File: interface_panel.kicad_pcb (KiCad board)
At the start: 2 copper layers, 165.1 x 33.4 mm, 48 parts, among them J1 Conn_01x04_Pin, J7 Conn_02x05_Odd_Even, J8 `, Q1 BC547, Q2 BC547, U1 SM420561N, U2 ATmega328P-P, U4 SM420561N, U7 TTP223-BA6, U8 TTP223-BA6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

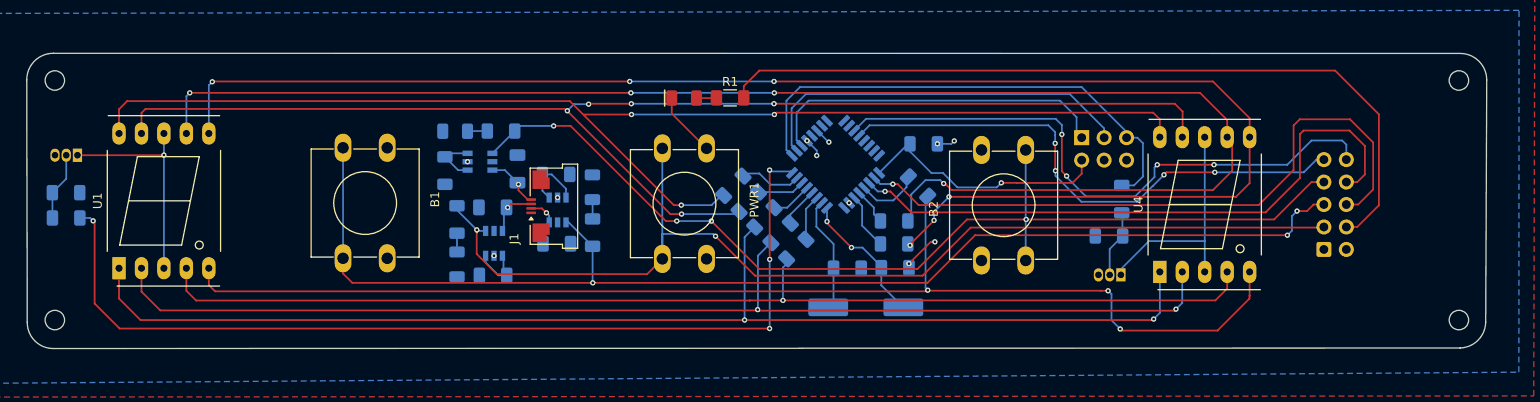
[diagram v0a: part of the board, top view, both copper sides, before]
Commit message: redimensioned
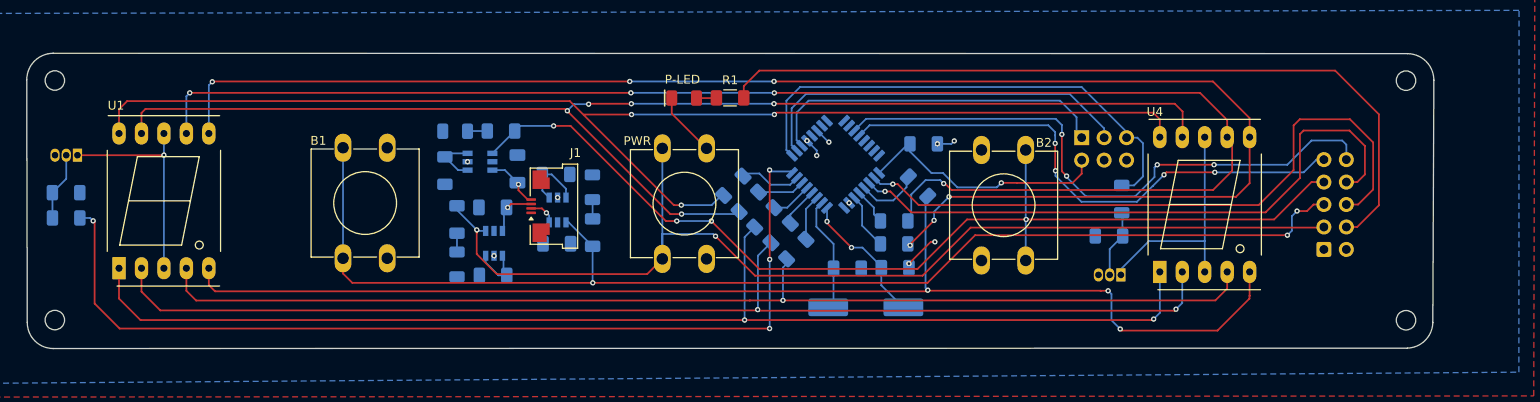
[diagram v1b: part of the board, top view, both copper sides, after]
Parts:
- B1: value SW_Push -> Heater1
- moved H2 5.98 mm to (209.1, 105.4)
- moved H3 5.98 mm to (209.1, 78.3)
- renumbered PWR1 to PWR
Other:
- board size 165.1 x 33.4 mm -> 159.2 x 33.4 mm
- board text added: "P-LED"

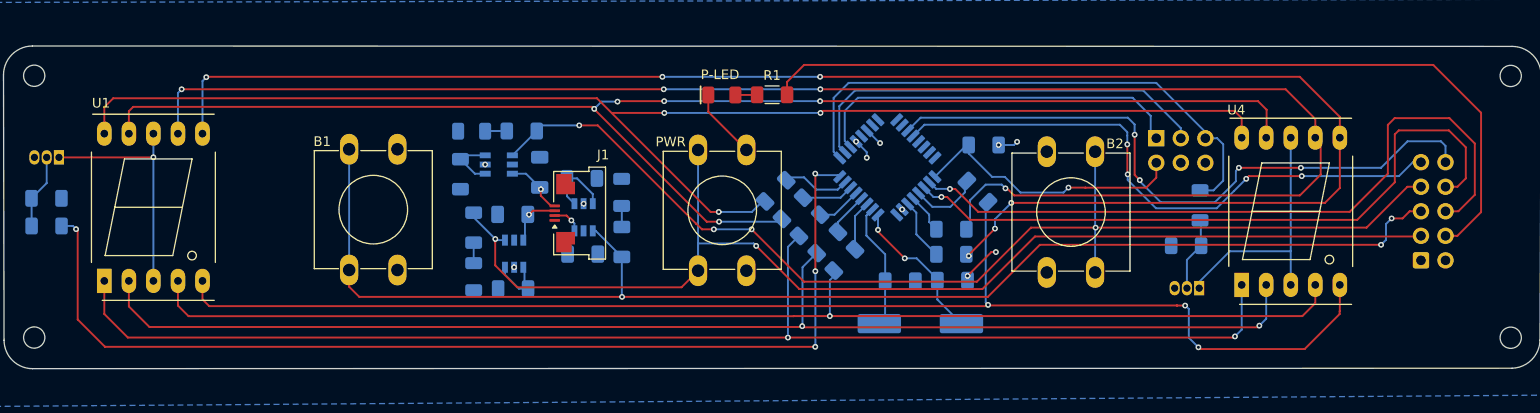
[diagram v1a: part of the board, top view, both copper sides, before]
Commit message: Fixed- schematics -atmega symbol
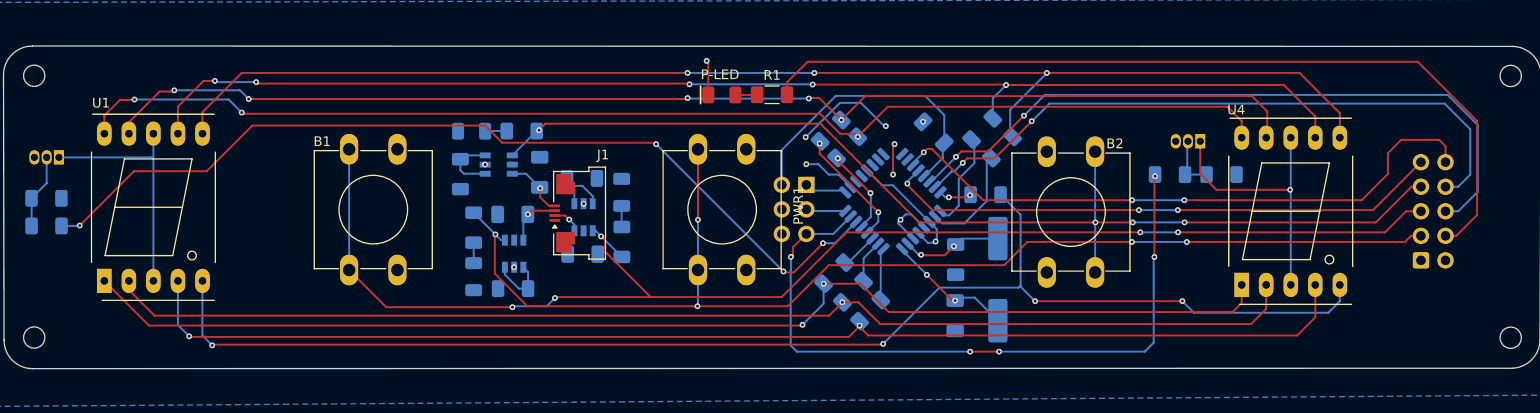
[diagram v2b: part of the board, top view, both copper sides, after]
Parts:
- removed PWR: SW_Push, Button_Switch_THT:SW_PUSH-12mm
- removed U2: ATmega328P-P, atmega328p-smd:QFP80P900X900X120-32N
- added PWR1: SW_Push, Button_Switch_THT:SW_PUSH-12mm, F.Cu at (130.0, 85.9)
- added U3: ATmega328P-A, Package_QFP:TQFP-32_7x7mm_P0.8mm, B.Cu at (145.2, 91.3)
- B1: value Heater1 -> SW_Push
- moved J8 36.5 mm to (136.2, 89.5), turned to 180 degrees
- moved Q2 15.2 mm to (177.0, 85.0)
- moved R8 12.2 mm to (156.4, 85.7), turned to 45 degrees
- moved R7 10.9 mm to (154.4, 83.8), turned to 45 degrees
- moved Y1 9.23 mm to (156.0, 99.3), turned to 90 degrees
- moved R12 8.96 mm to (138.7, 83.9), turned to 45 degrees
- moved R5 8.67 mm to (140.4, 85.7), turned to 45 degrees
- moved R14 8.22 mm to (179.2, 88.5), turned to 180 degrees
- moved C2 6.72 mm to (151.6, 103.1), turned to -90 degrees
- moved R9 5.88 mm to (142.8, 102.5)
- moved R10 5.76 mm to (141.0, 100.6)
- moved R11 5.57 mm to (139.1, 98.7)
- moved R2 5.34 mm to (149.4, 84.1), turned to -45 degrees
- moved R4 4.44 mm to (173.8, 88.5), turned to 0 degrees
- moved C1 2.18 mm to (151.7, 97.3), turned to -90 degrees
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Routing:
- net A: track 170.9 -> 129.4 mm, vias 4 -> 5
- net B: track 174.4 -> 134.0 mm, vias 6 -> 3
- net /miso: track 43.7 -> 4.09 mm
- net D13: track 40.2 -> 4.38 mm
- net F: track 148.1 -> 126.2 mm
- net G: track 144.4 -> 125.5 mm
- net 5V: track 4.18 -> 22.3 mm
- net /mosi: track 57.0 -> 73.1 mm, vias 0 -> 5
- net Net-(U3-PB2): track 109.2 -> 95.0 mm
- net E: track 138.1 -> 126.1 mm
- net D: track 133.4 -> 124.4 mm, vias 2 -> 1
- net Net-(U3-PB0): track 5.35 -> 12.5 mm, vias 0 -> 2
- net GND: track 13.2 -> 20.1 mm, vias 3 -> 4
- net Net-(U3-PD3): track 4.18 -> 10.3 mm
- net Net-(U3-XTAL1/PB6): track 15.9 -> 10.7 mm
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
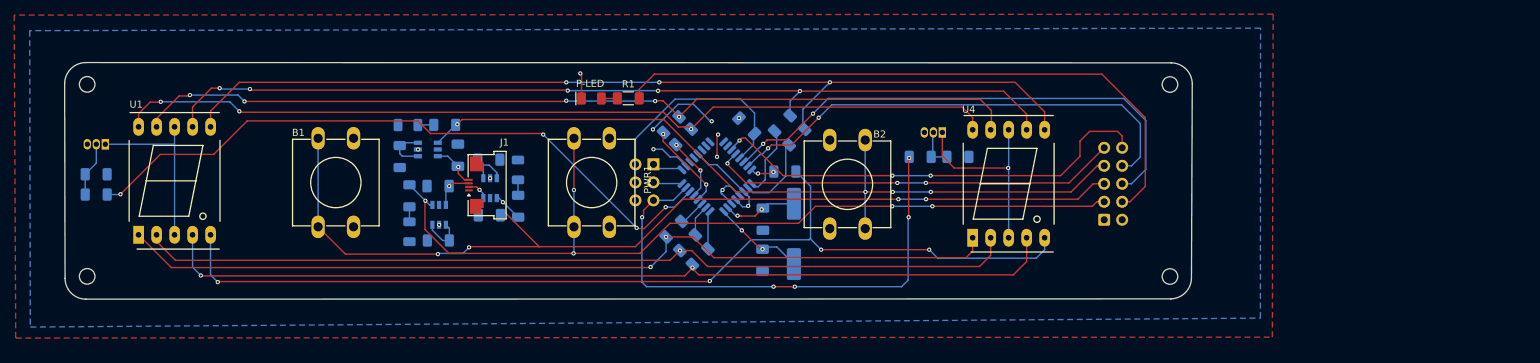
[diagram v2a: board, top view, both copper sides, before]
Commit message: fully routed with TH-atmega
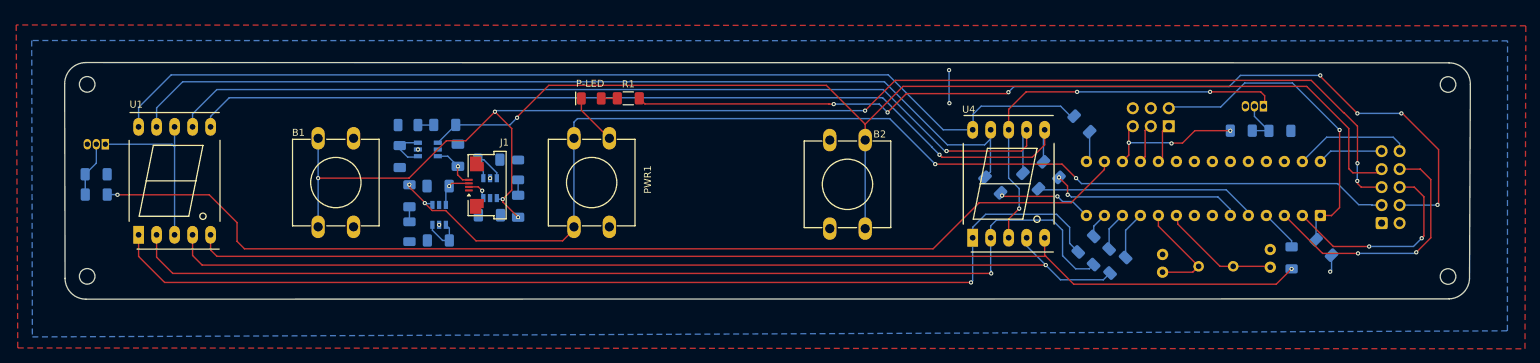
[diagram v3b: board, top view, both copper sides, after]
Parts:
- removed U3: ATmega328P-A, Package_QFP:TQFP-32_7x7mm_P0.8mm
- added U2: ATmega328P-P, Package_DIP:DIP-28_W7.62mm, B.Cu at (230.3, 96.8)
- C1, C2: footprint Capacitor_SMD:C_1206_3216Metric_Pad1.33x1.80mm_HandSolder -> Capacitor_THT:C_Disc_D3.0mm_W2.0mm_P2.50mm
- Y1: footprint Crystal:Crystal_SMD_HC49-SD -> Crystal:Crystal_HC49-U_Vertical
- moved R2 83.2 mm to (230.8, 101.2), turned to 135 degrees
- moved J8 72.9 mm to (208.9, 84.2), turned to 90 degrees
- moved R6 72.6 mm to (226.3, 102.7), turned to -90 degrees
- moved C1 71.9 mm to (223.3, 104.0), turned to 90 degrees
- moved R9 59.0 mm to (201.8, 103.8)
- moved R10 58.4 mm to (199.4, 102.6)
- moved R11 58.2 mm to (197.2, 100.8)
- moved Y1 57.3 mm to (213.2, 103.9), turned to 0 degrees
- moved C2 56.5 mm to (208.1, 104.8), turned to 90 degrees
- moved R5 56.3 mm to (196.7, 83.8), turned to 135 degrees
- moved R12 46.2 mm to (184.1, 92.5), turned to 135 degrees
- moved R14 45.6 mm to (224.6, 84.8)
- moved Q2 45.5 mm to (222.3, 81.3)
- moved R4 45.5 mm to (219.2, 84.8)
- moved H2 39.2 mm to (248.4, 105.4)
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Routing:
- net Net-(U2-PB2): track 95.0 -> 151.2 mm, vias 4 -> 1
- net /K1: track 142.1 -> 197.7 mm, vias 5 -> 7
- net /mosi: track 73.1 -> 21.4 mm, vias 5 -> 3
- net /K2: track 113.7 -> 164.5 mm, vias 4 -> 1
- net /A5: track 58.3 -> 9.26 mm, vias 3 -> 0
- net /A4: track 63.9 -> 17.2 mm, vias 3 -> 0
- net RX: track 72.8 -> 29.1 mm
- net S. LED: track 90.0 -> 133.5 mm, vias 0 -> 7
- net /K3: track 125.1 -> 163.0 mm, vias 5 -> 4
- net TX: track 67.9 -> 37.2 mm
- net Net-(Q2-C): track 28.6 -> 58.5 mm, vias 1 -> 3
- net D: track 124.4 -> 148.7 mm
- net E: track 126.1 -> 149.1 mm, vias 2 -> 1
- net Net-(U2-PD3): track 10.3 -> 31.5 mm
- net DPX: track 140.1 -> 160.3 mm, vias 4 -> 1
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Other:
- board size 159.2 x 33.4 mm -> 198.4 x 33.4 mm

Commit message: dimension plot
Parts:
- moved R6 9.93 mm to (216.7, 105.4)
- moved U2 9.93 mm to (220.8, 99.4)
- moved U4 9.93 mm to (171.7, 102.5)
- moved Y1 9.93 mm to (203.6, 106.6)
- moved J7 9.93 mm to (229.4, 100.5)
- moved PWR1 9.93 mm to (120.4, 88.5)
- moved Q2 9.93 mm to (212.7, 84.0)
- moved R10 9.93 mm to (189.8, 105.2)
- moved R4 9.93 mm to (209.6, 87.4)
- moved R5 9.93 mm to (187.1, 86.5)
- moved C6 9.93 mm to (103.5, 99.4)
- moved D1 9.93 mm to (117.8, 82.9)
- moved D5 9.93 mm to (107.5, 93.0)
- moved D6 9.93 mm to (92.0, 86.6)
- moved H1 9.93 mm to (46.7, 80.9)
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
